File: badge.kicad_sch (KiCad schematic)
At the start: 29 parts, among them J1 TC2030, SW1 SW_Push, SW2 SW_Push, SW3 SW_Push, SW4 SW_Push, SW5 SW_Push, SW6 SW_SPST, U1 NHD-C12832A1Z-FSRGB-FBW-3V, X1 Simple_Addon_v2

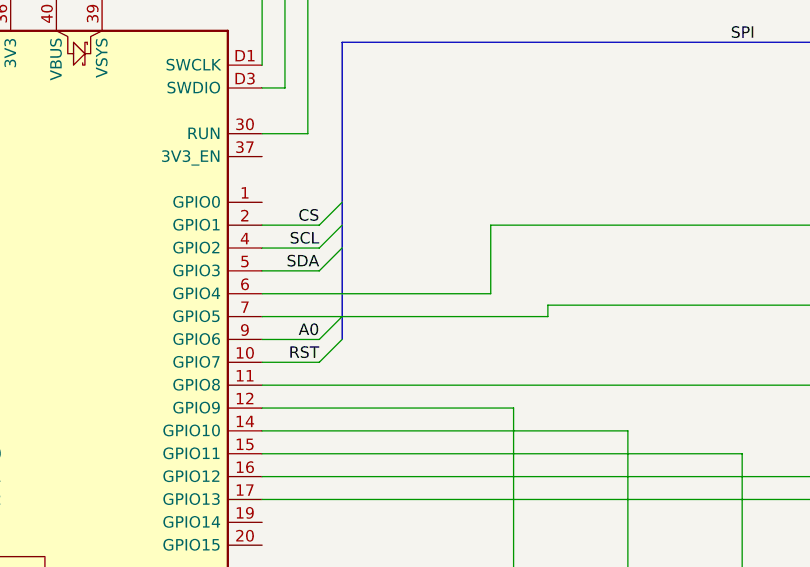
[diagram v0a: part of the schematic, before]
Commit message: swap A0 and the green LED
this way the backlight colors are all on channel A of different PWM
peripherals.
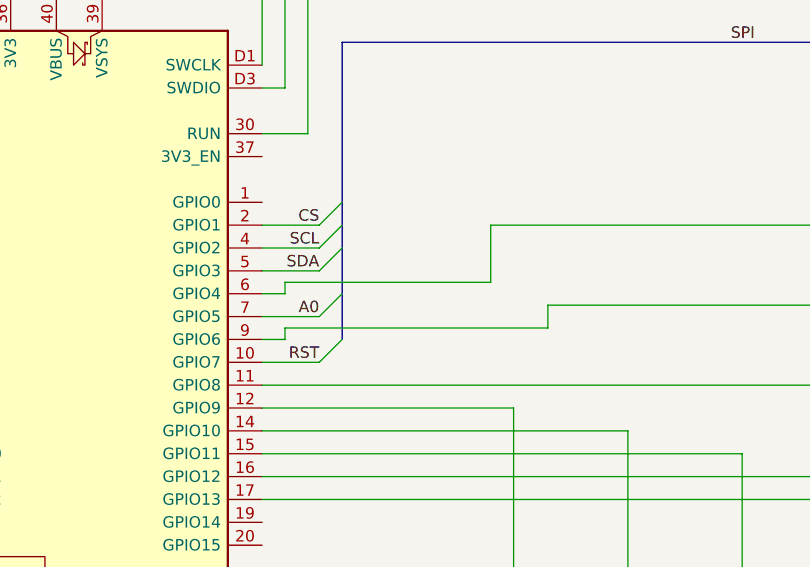
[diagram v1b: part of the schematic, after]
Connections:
- net A0: now also A1.7 (GPIO5); no longer A1.9 (GPIO6)
- net at R2.1: now also A1.9 (GPIO6); no longer A1.7 (GPIO5)
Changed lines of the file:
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@@
 	)
 	(bus_entry
-		(at 148.59 130.81)
+		(at 148.59 128.27)
 		(size -2.54 2.54)
 		(stroke
@@
 	(wire
 		(pts
+			(xy 171.45 129.54) (xy 171.45 132.08)
+		)
+		(stroke
+			(width 0)
+			(type default)
+		)
+	)
+	(wire
+		(pts
 			(xy 176.53 46.99) (xy 172.72 46.99)
 		)
@@
 	(wire
 		(pts
-			(xy 165.1 120.65) (xy 165.1 128.27)
+			(xy 165.1 120.65) (xy 165.1 127)
+		)
+		(stroke
+			(width 0)
+			(type default)
+		)
+	)
+	(wire
+		(pts
+			(xy 142.24 133.35) (xy 139.7 133.35)
 		)
 		(stroke
@@
 	(wire
 		(pts
-			(xy 171.45 129.54) (xy 171.45 130.81)
-		)
-		(stroke
-			(width 0)
-			(type default)
-		)
-	)
-	(wire
-		(pts
 			(xy 92.71 43.18) (xy 92.71 57.15)
 		)
@@
 	(wire
 		(pts
+			(xy 142.24 127) (xy 142.24 128.27)
+		)
+		(stroke
+			(width 0)
+			(type default)
+		)
+	)
+	(wire
+		(pts
 			(xy 139.7 123.19) (xy 146.05 123.19)
 		)
@@
 	(wire
 		(pts
-			(xy 139.7 130.81) (xy 171.45 130.81)
-		)
-		(stroke
-			(width 0)
-			(type default)
-		)
-	)
-	(wire
-		(pts
 			(xy 168.91 72.39) (xy 165.1 72.39)
 		)
@@
 	(wire
 		(pts
-			(xy 139.7 128.27) (xy 165.1 128.27)
+			(xy 142.24 127) (xy 165.1 127)
 		)
 		(stroke
@@
 	(wire
 		(pts
+			(xy 142.24 132.08) (xy 142.24 133.35)
+		)
+		(stroke
+			(width 0)
+			(type default)
+		)
+	)
+	(wire
+		(pts
 			(xy 36.83 170.18) (xy 167.64 170.18)
 		)
@@
 	(wire
 		(pts
+			(xy 142.24 128.27) (xy 139.7 128.27)
+		)
+		(stroke
+			(width 0)
+			(type default)
+		)
+	)
+	(wire
+		(pts
+			(xy 171.45 132.08) (xy 142.24 132.08)
+		)
+		(stroke
+			(width 0)
+			(type default)
+		)
+	)
+	(wire
+		(pts
 			(xy 66.04 165.1) (xy 66.04 170.18)
 		)
@@
 	(wire
 		(pts
-			(xy 139.7 133.35) (xy 146.05 133.35)
+			(xy 139.7 130.81) (xy 146.05 130.81)
 		)
 		(stroke
@@
 	)
 	(label "A0"
-		(at 146.05 133.35 180)
+		(at 146.05 130.81 180)
 		(effects
 			(font

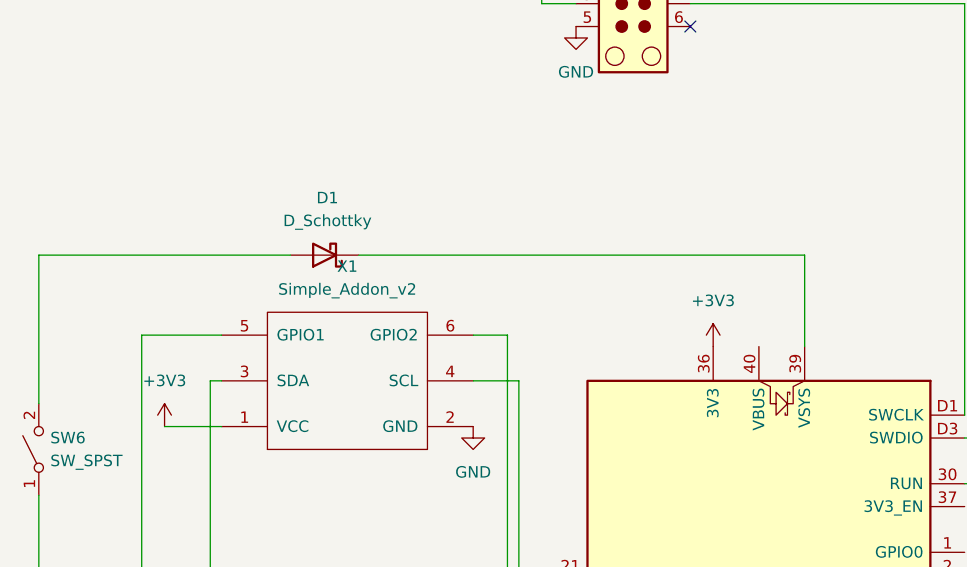
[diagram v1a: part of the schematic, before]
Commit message: SAO silkscreens, nudge a few vias around
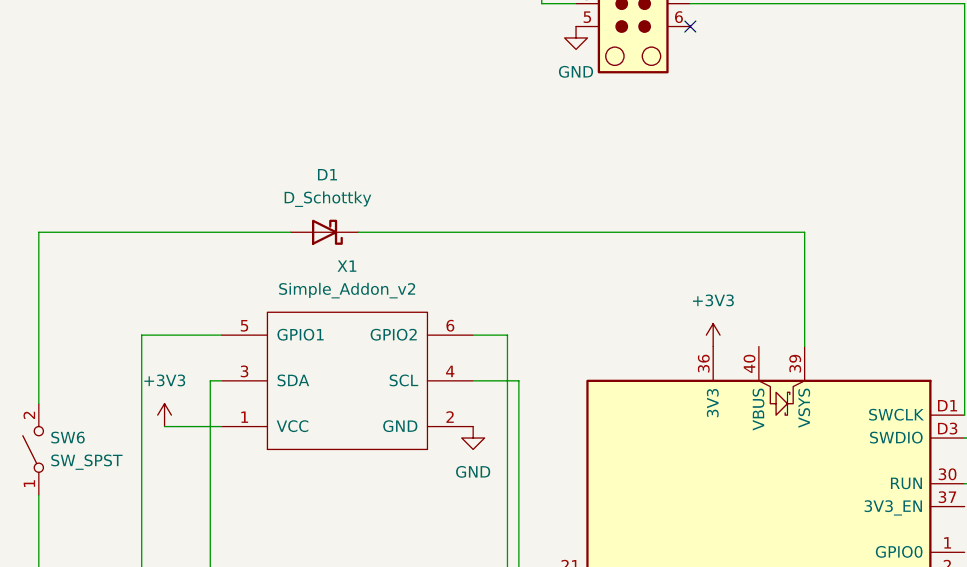
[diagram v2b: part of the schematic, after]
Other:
- moved on the sheet: D1
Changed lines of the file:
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@@
 	(wire
 		(pts
-			(xy 36.83 101.6) (xy 36.83 85.09)
+			(xy 36.83 101.6) (xy 36.83 82.55)
 		)
 		(stroke
@@
 	(wire
 		(pts
-			(xy 121.92 85.09) (xy 121.92 95.25)
+			(xy 121.92 82.55) (xy 121.92 95.25)
 		)
 		(stroke
@@
 	(wire
 		(pts
-			(xy 36.83 85.09) (xy 64.77 85.09)
+			(xy 36.83 82.55) (xy 64.77 82.55)
 		)
 		(stroke
@@
 	(wire
 		(pts
-			(xy 72.39 85.09) (xy 121.92 85.09)
+			(xy 72.39 82.55) (xy 121.92 82.55)
 		)
 		(stroke
@@
 	(symbol
 		(lib_id "Device:D_Schottky")
-		(at 68.58 85.09 180)
+		(at 68.58 82.55 180)
 		(unit 1)
 		(body_style 1)
@@
 		(fields_autoplaced yes)
 		(property "Reference" "D1"
+			(at 68.8975 76.2 0)
+			(show_name no)
+			(do_not_autoplace no)
+			(effects
+				(font
+					(size 1.27 1.27)
+				)
+			)
+		)
+		(property "Value" "D_Schottky"
 			(at 68.8975 78.74 0)
 			(show_name no)
@@
 			)
 		)
-		(property "Value" "D_Schottky"
-			(at 68.8975 81.28 0)
-			(show_name no)
-			(do_not_autoplace no)
-			(effects
-				(font
-					(size 1.27 1.27)
-				)
-			)
-		)
 		(property "Footprint" "Diode_THT:D_DO-35_SOD27_P10.16mm_Horizontal"
-			(at 68.58 85.09 0)
+			(at 68.58 82.55 0)
 			(hide yes)
 			(show_name no)
@@
 		)
 		(property "Datasheet" ""
-			(at 68.58 85.09 0)
+			(at 68.58 82.55 0)
 			(hide yes)
 			(show_name no)
@@
 		)
 		(property "Description" "Schottky diode"
-			(at 68.58 85.09 0)
+			(at 68.58 82.55 0)
 			(hide yes)
 			(show_name no)

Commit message: make LEDs 5mm, move them apart, nudge traces around
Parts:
- D2, D3, D4: footprint LED_THT:LED_D3.0mm -> LED_THT:LED_D5.0mm
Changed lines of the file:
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@@
 			)
 		)
-		(property "Footprint" "LED_THT:LED_D3.0mm"
+		(property "Footprint" "LED_THT:LED_D5.0mm"
 			(at 78.74 161.29 0)
 			(hide yes)
@@
 			)
 		)
-		(property "Footprint" "LED_THT:LED_D3.0mm"
+		(property "Footprint" "LED_THT:LED_D5.0mm"
 			(at 72.39 161.29 0)
 			(hide yes)
@@
 			)
 		)
-		(property "Footprint" "LED_THT:LED_D3.0mm"
+		(property "Footprint" "LED_THT:LED_D5.0mm"
 			(at 66.04 161.29 0)
 			(hide yes)
